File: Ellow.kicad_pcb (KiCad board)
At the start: 2 copper layers, 20.5 x 36.8 mm, 26 parts, among them J1 USB_C_Receptacle_USB2.0, J2 M_2_AKey_KB, J3 Conn_01x02_Female, J5 Conn_01x04_Female, Q1 A03407, Q2 A03407, U1 AP2112K-3.3, U2 E73-2G4M08S1C, U3 LN2054Y42AMR, Y1 32.768kHz

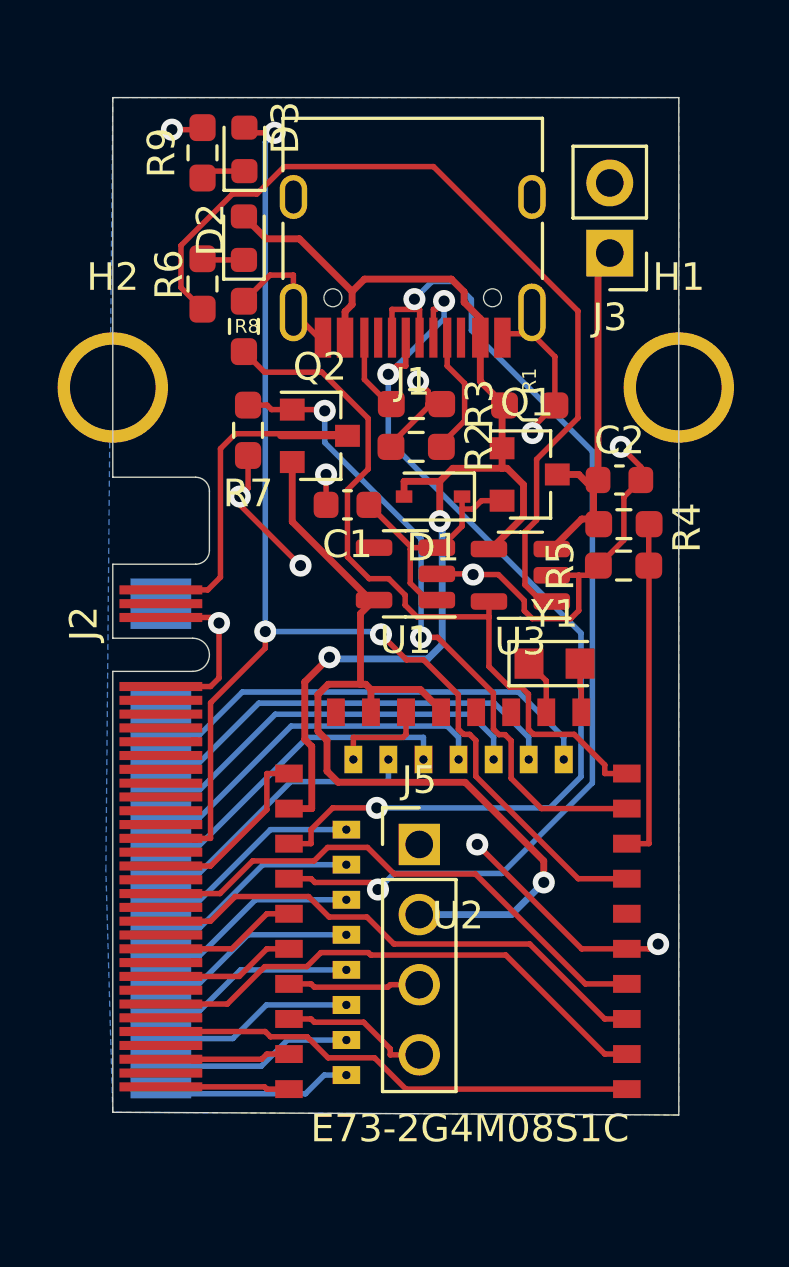
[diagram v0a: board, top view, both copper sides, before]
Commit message: first autoroute attempt
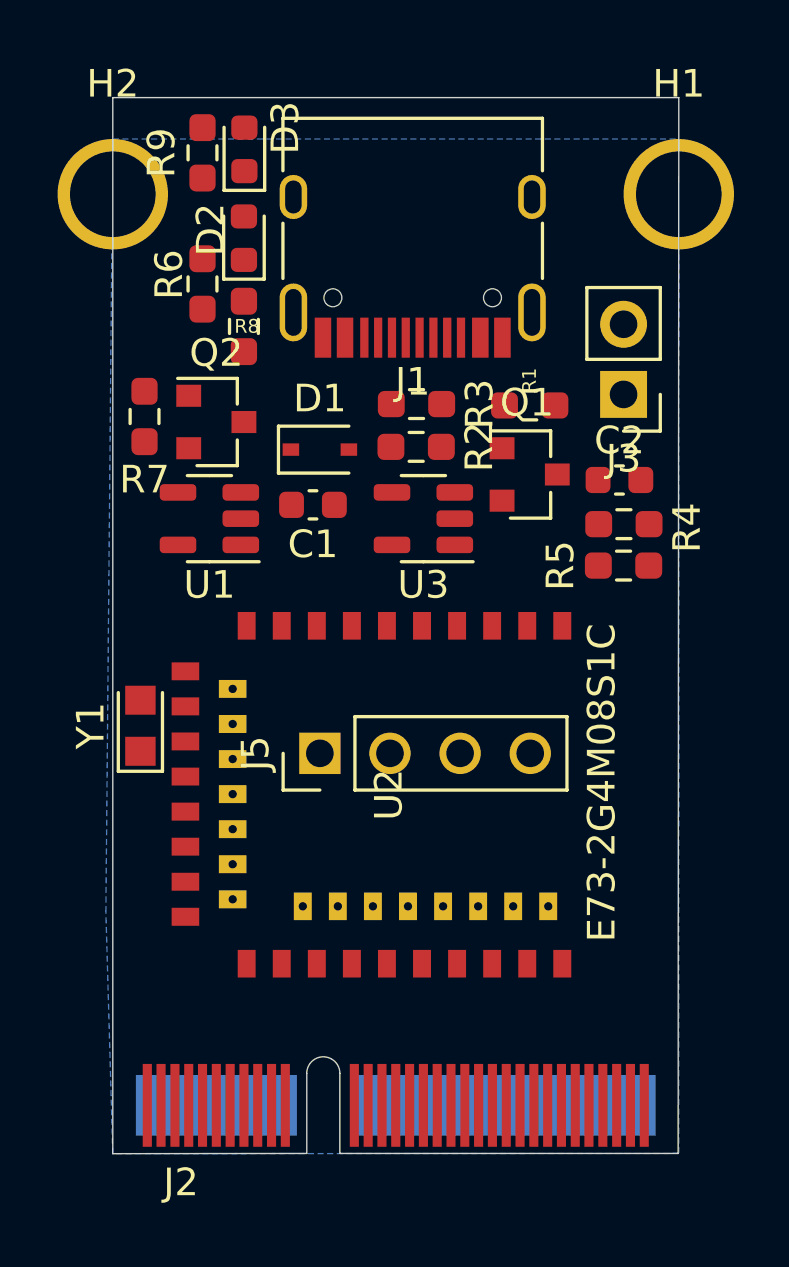
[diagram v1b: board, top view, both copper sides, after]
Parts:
- J2: value M_2_AKey_KB -> 2199119-4; footprint ellow:M_2_EdgeConnector_A_Key -> ellow:M_2_EdgeConnector_E_Key
- moved J2 15.3 mm to (235.5, 130.8), turned to 0 degrees
- moved Y1 15.2 mm to (226.3, 115.3), turned to 90 degrees
- moved U2 10.8 mm to (227.5, 117.8), turned to 0 degrees
- moved U1 7.38 mm to (228.8, 107.8)
- moved H1 7.00 mm to (245.8, 96.1)
- moved H2 7.00 mm to (225.3, 96.1)
- moved J3 5.14 mm to (243.8, 103.3)
- moved J5 4.88 mm to (232.8, 116.3), turned to 90 degrees
- moved D1 4.44 mm to (232.8, 105.3), turned to 0 degrees
- moved U3 4.07 mm to (236.5, 107.8)
- moved Q2 3.78 mm to (229.0, 104.3)
- moved R7 3.78 mm to (226.4, 104.1)
- moved C1 1.25 mm to (232.5, 107.3)
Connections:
- J2 pad 16: GND -> Net-(J2-Pad16)
- J2 pad 19: Net-(J2-Pad19) -> P0.06
- J2 pad 23: P0.26 -> P0.08
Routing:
- net GND: track 54.8 -> 0.00 mm, vias 11 -> 0
- net P0.02: track 47.8 -> 0.00 mm, vias 3 -> 0
- net VBUS: track 43.6 -> 0.00 mm, vias 2 -> 0
- net DATA+: track 38.1 -> 0.00 mm, vias 2 -> 0
- net DATA-: track 36.2 -> 0.00 mm, vias 3 -> 0
- net VDD_H: track 33.5 -> 0.00 mm, vias 1 -> 0
- net Net-(R6-Pad2): track 32.3 -> 0.00 mm
- net PROG: track 27.0 -> 0.00 mm
- net EXT_VCC_CONTROL: track 24.1 -> 0.00 mm, vias 2 -> 0
- net P0.28: track 19.6 -> 0.00 mm
- net P1.10: track 19.2 -> 0.00 mm
- net P0.03: track 19.1 -> 0.00 mm
- net P1.11: track 17.7 -> 0.00 mm
- net P0.26: track 16.7 -> 0.00 mm
- net P0.06: track 15.5 -> 0.00 mm
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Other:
- board size 20.5 x 36.8 mm -> 20.5 x 38.2 mm

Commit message: routed and ready for QA check
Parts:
- added SW1: SW_Push, Button_Switch_SMD:SW_SPST_B3U-1000P, F.Cu at (244.0, 100.1)
- J2, R2, R3: moved to B.Cu
- moved J3 17.1 mm to (226.7, 103.2)
- moved C1 12.1 mm to (244.4, 104.8)
- moved D1 11.7 mm to (244.3, 103.1)
- moved R9 9.92 mm to (230.1, 104.4), turned to 270 degrees
- moved R2 8.58 mm to (237.4, 96.7), turned to 90 degrees
- moved R7 7.13 mm to (233.6, 104.4)
- moved R3 7.07 mm to (235.1, 96.7), turned to 90 degrees
- moved R6 5.97 mm to (231.7, 104.4)
- moved Q1 4.36 mm to (236.5, 108.1), turned to 180 degrees
- moved Q2 3.66 mm to (226.6, 107.0), turned to 180 degrees
- moved U3 3.31 mm to (236.7, 104.5), turned to 0 degrees
- moved U1 2.58 mm to (231.4, 108.0)
- moved R5 2.50 mm to (245.0, 107.3), turned to 90 degrees
- moved C2 2.10 mm to (241.7, 105.7), turned to 90 degrees
- moved Y1 1.44 mm to (227.0, 114.1)
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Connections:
- J1 pad A8: Net-(J1-PadA8) -> (no net)
- J1 pad B8: Net-(J1-PadB8) -> (no net)
- J2 pad 1: Net-(J2-Pad1) -> P0.10
- J2 pad 10: Net-(J2-Pad10) -> P1.06
- J2 pad 11: Net-(J2-Pad11) -> (no net)
- J2 pad 12: Net-(J2-Pad12) -> (no net)
- J2 pad 13: Net-(J2-Pad13) -> P1.10
- J2 pad 14: Net-(J2-Pad14) -> P1.04
- J2 pad 15: P0.26 -> (no net)
- J2 pad 16: Net-(J2-Pad16) -> (no net)
- J2 pad 17: Net-(J2-Pad17) -> P0.24
- J2 pad 18: Net-(J2-Pad18) -> P1.02
- J2 pad 19: P0.06 -> (no net)
- J2 pad 2: EXT_VCC -> (no net)
- J2 pad 20: Net-(J2-Pad20) -> (no net)
- J2 pad 21: Net-(J2-Pad21) -> P0.13
- J2 pad 22: Net-(J2-Pad22) -> P1.00
- J2 pad 23: P0.08 -> (no net)
- J2 pad 3: Net-(J2-Pad3) -> (no net)
- J2 pad 32: Net-(J2-Pad32) -> P0.22
- J2 pad 33: Net-(J2-Pad33) -> P0.28
- J2 pad 34: Net-(J2-Pad34) -> (no net)
- J2 pad 35: P0.04 -> (no net)
- J2 pad 36: Net-(J2-Pad36) -> P0.20
- J2 pad 37: Net-(J2-Pad37) -> P0.02
- J2 pad 38: P0.02 -> (no net)
- J2 pad 39: P0.12 -> (no net)
- J2 pad 4: Net-(J2-Pad4) -> (no net)
- J2 pad 40: Net-(J2-Pad40) -> P0.17
- J2 pad 41: Net-(J2-Pad41) -> (no net)
- J2 pad 42: RESET -> (no net)
- J2 pad 43: P0.07 -> (no net)
- J2 pad 44: Net-(J2-Pad44) -> P0.15
- J2 pad 45: Net-(J2-Pad45) -> (no net)
- J2 pad 46: P0.28 -> (no net)
- J2 pad 47: P0.15 -> (no net)
- J2 pad 48: Net-(J2-Pad48) -> P0.07
- J2 pad 49: Net-(J2-Pad49) -> (no net)
- J2 pad 5: Net-(J2-Pad5) -> P0.09
- J2 pad 50: P0.03 -> (no net)
- J2 pad 51: P0.17 -> (no net)
- J2 pad 52: Net-(J2-Pad52) -> P0.12
- J2 pad 53: Net-(J2-Pad53) -> (no net)
- J2 pad 54: P0.13 -> (no net)
- J2 pad 55: P0.20 -> (no net)
- J2 pad 56: Net-(J2-Pad56) -> P0.04
- J2 pad 57: Net-(J2-Pad57) -> RESET
- J2 pad 58: P0.24 -> (no net)
- J2 pad 59: P0.22 -> (no net)
- J2 pad 6: GND -> (no net)
- J2 pad 60: Net-(J2-Pad60) -> P0.08
- J2 pad 61: Net-(J2-Pad61) -> (no net)
- J2 pad 62: P1.10 -> (no net)
- J2 pad 63: P1.00 -> (no net)
- J2 pad 64: Net-(J2-Pad64) -> P0.06
- J2 pad 65: Net-(J2-Pad65) -> (no net)
- J2 pad 66: P1.11 -> (no net)
- J2 pad 67: P1.02 -> (no net)
- J2 pad 68: Net-(J2-Pad68) -> P0.26
- J2 pad 69: Net-(J2-Pad69) -> (no net)
- J2 pad 7: Net-(J2-Pad7) -> (no net)
- J2 pad 70: P0.09 -> (no net)
- J2 pad 71: P1.04 -> (no net)
- J2 pad 72: Net-(J2-Pad72) -> (no net)
- J2 pad 73: Net-(J2-Pad73) -> (no net)
- J2 pad 74: P0.10 -> EXT_VCC
- J2 pad 75: P1.06 -> GND
- J2 pad 8: Net-(J2-Pad8) -> (no net)
- J2 pad 9: Net-(J2-Pad9) -> P1.11
- U1 pad 4: Net-(U1-Pad4) -> (no net)
- U2 pad 15: P0.05 -> (no net)
- U2 pad 17: P1.09 -> (no net)
- U2 pad 25: DCCH -> (no net)
- U2 pad 3: P0.03 -> (no net)
- U2 pad 6: P1.13 -> (no net)
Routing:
- net VBUS: track 0.00 -> 55.9 mm, vias 0 -> 4
- net P0.02: track 0.00 -> 49.3 mm
- net RESET: track 0.00 -> 41.2 mm, vias 0 -> 2
- net GND: track 0.00 -> 37.0 mm, vias 0 -> 11
- net VDD_H: track 0.00 -> 33.1 mm, vias 0 -> 2
- net DATA+: track 0.00 -> 32.7 mm, vias 0 -> 2
- net PROG: track 0.00 -> 31.4 mm, vias 0 -> 3
- net VBAT: track 0.00 -> 28.6 mm, vias 0 -> 2
- net DATA-: track 0.00 -> 27.9 mm, vias 0 -> 4
- net P0.28: track 0.00 -> 25.5 mm
- net EXT_VCC: track 0.00 -> 22.5 mm, vias 0 -> 1
- net Net-(C1-Pad1): track 0.00 -> 20.5 mm
- net P1.10: track 0.00 -> 19.7 mm
- net P1.11: track 0.00 -> 19.1 mm
- net EXT_VCC_CONTROL: track 0.00 -> 18.5 mm, vias 0 -> 2
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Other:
- board size 20.5 x 38.2 mm -> 22.2 x 38.1 mm
- net class Power added: clearance 0.25, trace_width 0.25, via_dia 0.8, via_drill 0.4
